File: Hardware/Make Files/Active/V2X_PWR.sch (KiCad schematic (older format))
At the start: 69 parts, among them P10 Board Mount 2, P11 Ficudial2, P12 Board Mount 3, P13 Ficudial3, P14 USB_A, P15 Board Mount 4, P16 Ficudial4, P17 NVM_RST, P18 NVM_RST, P19 NVM_RST, P6 Board Mount 1, P7 Ficudial1, P8 Open Source, P9 USB_u, Q11 IRF9335, Q12 IRF9335, Q13 BSS84, Q14 IRF9335, Q15 2N7000, SW2 SW_PUSH, U11 XRP6124, U12 SLG59M, U13 SLG59M, U14 XRP6124, U15 SLG59M, U16 SLG59M, U17 XRP6124, U18 SLG59M

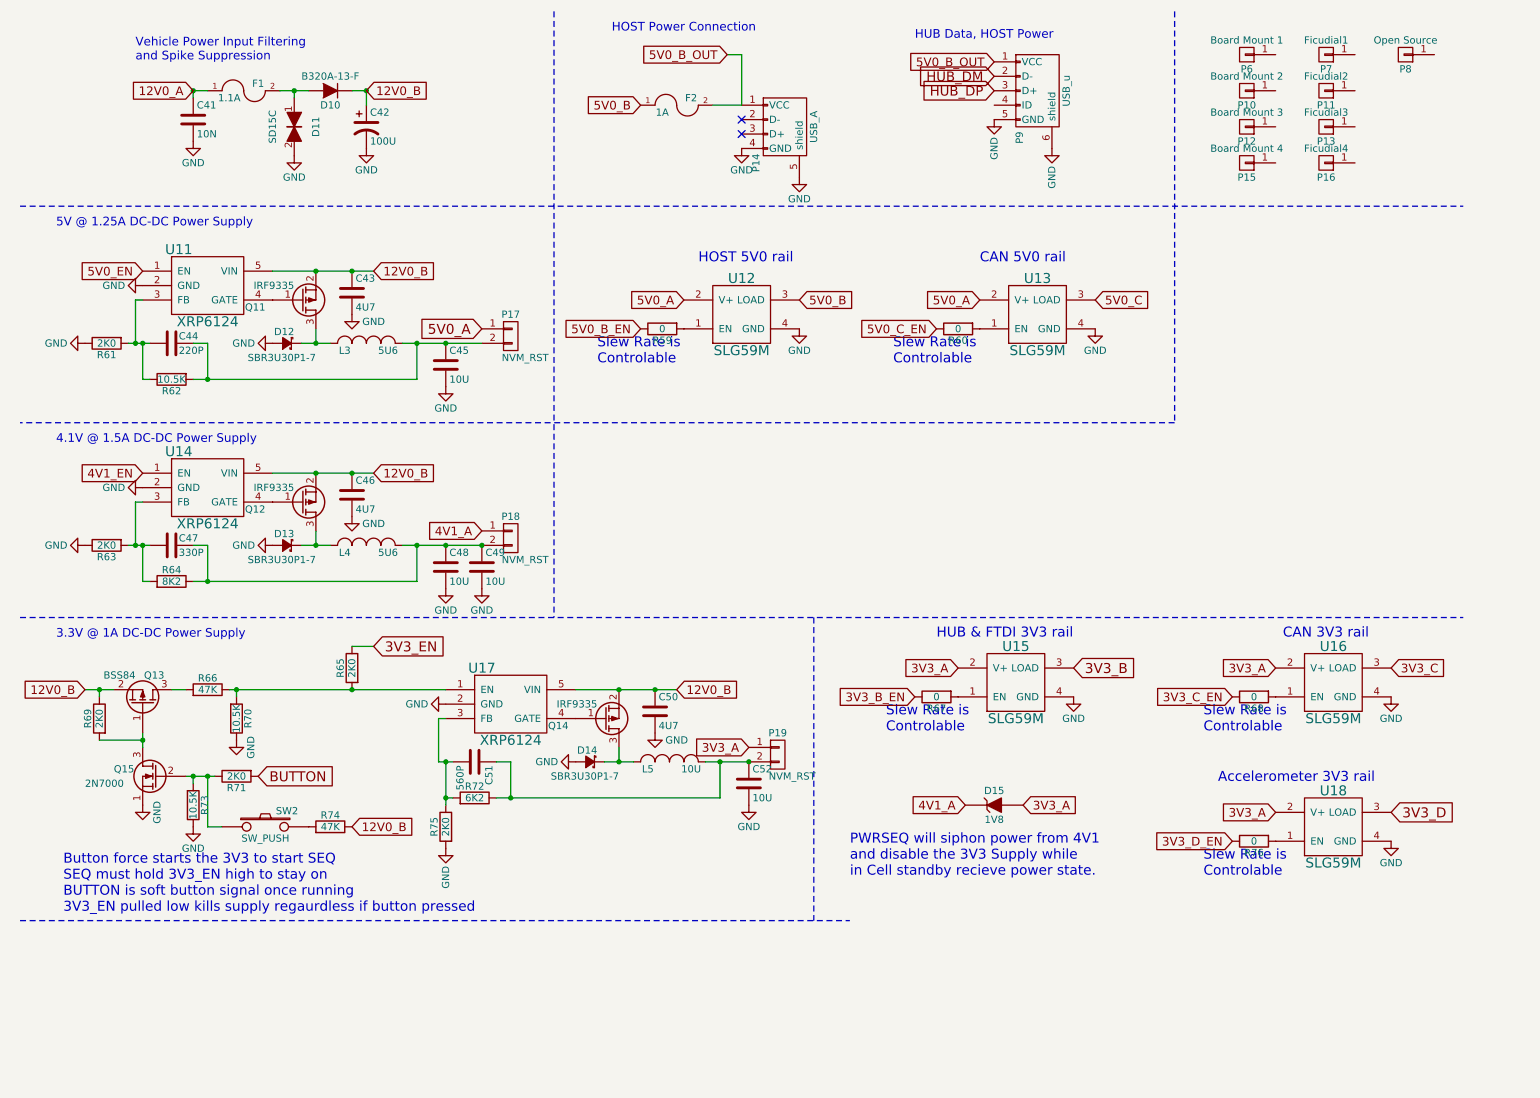
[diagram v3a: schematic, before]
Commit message: Split V2X in 2 boards, layout of SIM pcb done
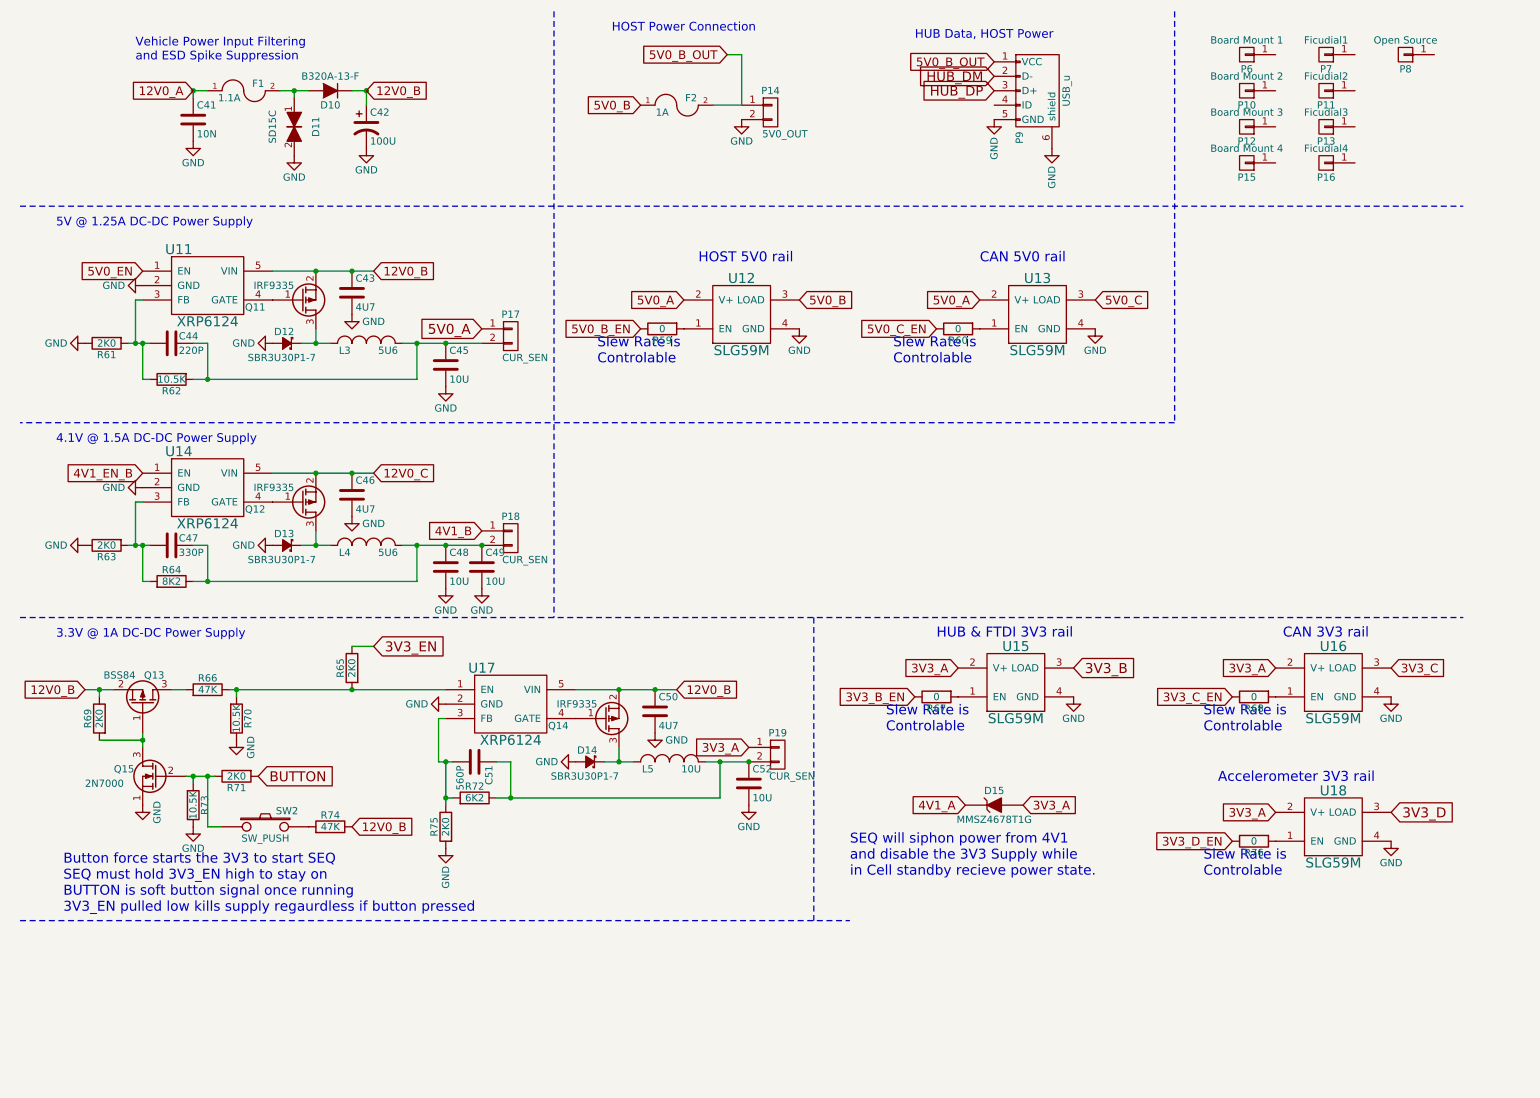
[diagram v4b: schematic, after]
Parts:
- removed P14: USB_A, Connect:USB_A, symbol USB_A
- added P14: 5V0_OUT, Connect:PINHEAD1-2, symbol CONN_01X02
- C41, C51: footprint Capacitors_SMD:C_0603 -> Custom Parts:C_0603_SM
- C43, C46, C50: footprint Capacitors_SMD:C_0603 -> Custom Parts:C_0805_SM
- C44, C47: footprint Capacitors_SMD:C_1210 -> Custom Parts:C_0603_SM
- C45, C48, C49, C52: footprint Capacitors_SMD:C_1210 -> Custom Parts:C_1206_SM
- D10: footprint Diodes_SMD:Diode-SMC_Standard -> Diodes_SMD:SMA_Standard
- D12, D13, D14: footprint (none) -> Diodes_SMD:SOD-123
- D15: value 1V8 -> MMSZ4678T1G; footprint (none) -> Diodes_SMD:SOD-123
- F2: footprint Resistors_SMD:R_1210 -> Resistors_SMD:R_1812
- L3, L4, L5: footprint (none) -> Custom Parts:4.5x4.5mm_Ind
- P17, P18, P19: value NVM_RST -> CUR_SEN
- P9: footprint Connect:USB_Micro-B -> Custom Parts:USB_Micro-B-DX4R005JJ2R1800
- Q11, Q12, Q14: footprint (none) -> Custom Parts:SOIC-8_MOS
- Q15: footprint (none) -> Housings_SOT-23_SOT-143_TSOT-6:SOT-23
- R59, R60, R61, R62, R63, R64, R65, R66, R67, R68, R69, R70, R71, R72, R73, R74, R75, R76: footprint Resistors_SMD:R_0603 -> Custom Parts:R_0603_sm
- SW2: footprint (none) -> Custom Parts:SW_SPST_FSMSM_SM
- U11, U14, U17: footprint (none) -> Housings_SOT-23_SOT-143_TSOT-6:SOT-23-5
- U12, U13, U15, U16, U18: footprint (none) -> Custom Parts:STDFN-4
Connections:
- net 12V0_B: no longer C46.1, Q12.2 (S), U14.5 (VIN)
- net 4V1_A: no longer P18.1 (P1)
- net 5V0_B_OUT: now also P14.1 (P1)
- net GND: now also P14.2 (P2)
- net 4V1_EN renamed 4V1_EN_B
- new net 12V0_C: C46.1, Q12.2 (S), U14.5 (VIN)
- new net 4V1_B: P18.1 (P1)
- no-connect marks 2 -> 0
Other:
- note added: "SEQ will siphon power from 4V1\nand disable the 3V3 Supply while \nin Cell standby recieve power state."
- note added: "Vehicle Power Input Filtering\nand ESD Spike Suppression"
- note removed: "PWRSEQ will siphon power from 4V1\nand disable the 3V3 Supply while \nin Cell standby recieve power state."
- note removed: "Vehicle Power Input Filtering\nand Spike Suppression"

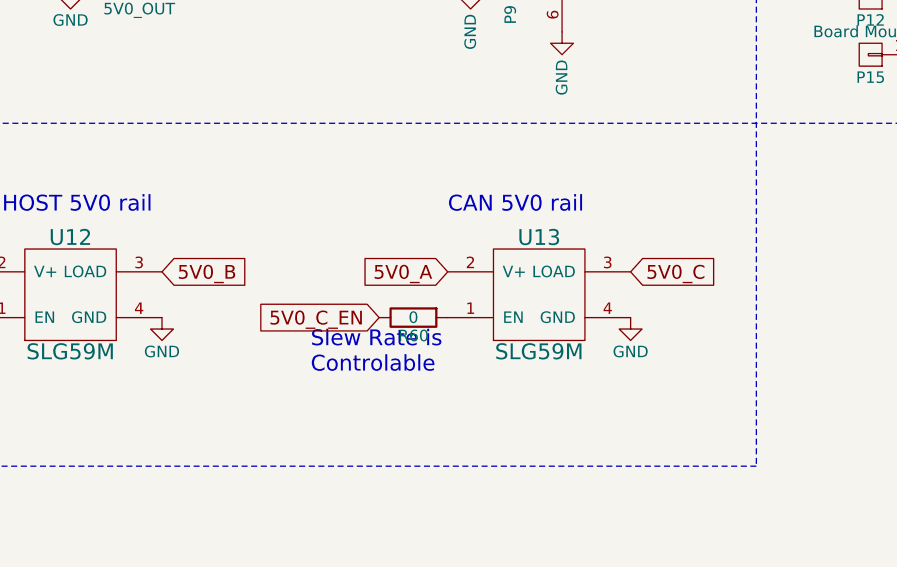
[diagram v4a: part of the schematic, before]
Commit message: Build pass of main V2X board
ready to verify
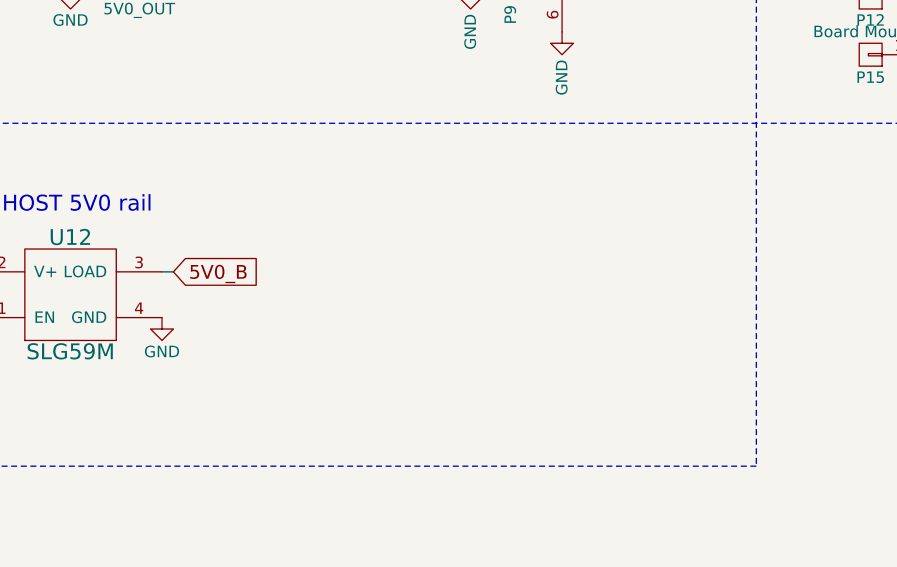
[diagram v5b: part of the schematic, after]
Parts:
- removed R60: 0, Custom Parts:R_0603_sm, symbol R
- removed U13: SLG59M, Custom Parts:STDFN-4, symbol SLG59M
- Q13, Q15: footprint Housings_SOT-23_SOT-143_TSOT-6:SOT-23 -> Custom Parts:SOT-23-123
- SW2: footprint Custom Parts:SW_SPST_FSMSM_SM -> Custom Parts:PTS645VK58-2-LFS
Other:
- note removed: "CAN 5V0 rail"
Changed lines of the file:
@@
 F 0 "SW2" H 2350 6260 50  0000 C CNN
 F 1 "SW_PUSH" H 2200 6070 50  0000 C CNN
-F 2 "Custom Parts:SW_SPST_FSMSM_SM" H 2200 6150 60  0001 C CNN
+F 2 "Custom Parts:PTS645VK58-2-LFS" H 2200 6150 60  0001 C CNN
 F 3 "http://www.mouser.com/ds/2/418/NG_CD_1437566-3_C2_1437566_3_1_c.dwg-116271.pdf" H 2200 6150 60  0001 C CNN
 F 4 "506-FSMSM" H 2200 6150 60  0001 C CNN "Mouse PN"
@@
 Text GLabel 950  5200 0    60   Input ~ 0
 12V0_B
-Text GLabel 5900 2500 2    60   Input ~ 0
+Text GLabel 5950 2500 2    60   Input ~ 0
 5V0_B
 Text GLabel 4800 1150 0    60   Input ~ 0
@@
 Text Notes 9250 4850 0    69   ~ 0
 CAN 3V3 rail
-Text GLabel 7150 2500 0    60   Input ~ 0
-5V0_A
-Text GLabel 6850 2700 0    60   Input ~ 0
-5V0_C_EN
-$Comp
-L GND #PWR0127
-U 1 1 5602FEC6
-P 7950 2700
-F 0 "#PWR0127" H 7950 2450 50  0001 C CNN
-F 1 "GND" H 7950 2550 50  0000 C CNN
-F 2 "" H 7950 2700 60  0000 C CNN
-F 3 "" H 7950 2700 60  0000 C CNN
-	1    7950 2700
-	1    0    0    -1
-$EndComp
-Text GLabel 7950 2500 2    60   Input ~ 0
-5V0_C
-Text Notes 6550 2950 0    69   ~ 0
-Slew Rate is\nControlable
-Text Notes 7150 2250 0    69   ~ 0
-CAN 5V0 rail
 Text Notes 5200 2250 0    69   ~ 0
 HOST 5V0 rail
@@
 $EndComp
 $Comp
-L SLG59M U13
-U 1 1 56056DDD
-P 7550 2600
-F 0 "U13" H 7550 2350 69  0000 C CNN
-F 1 "SLG59M" H 7550 2850 69  0000 C CNN
-F 2 "Custom Parts:STDFN-4" H 7550 2600 69  0001 C CNN
-F 3 "http://www.mouser.com/ds/2/665/SLG59M1440r111_12112013-463792.pdf" H 7550 2600 69  0001 C CNN
-F 4 "402-SLG59M1440V" H 7550 2600 60  0001 C CNN "Mouse PN"
-	1    7550 2600
-	1    0    0    1
-$EndComp
-$Comp
 L CONN_01X02 P19
 U 1 1 5607345C
@@
 $EndComp
 $Comp
-L R R60
-U 1 1 5607F2D8
-P 7000 2700
-F 0 "R60" V 7080 2700 50  0000 C CNN
-F 1 "0" V 7000 2700 50  0000 C CNN
-F 2 "Custom Parts:R_0603_sm" V 6930 2700 30  0001 C CNN
-F 3 "http://www.mouser.com/ds/2/427/dcrcwe3-109170.pdf" H 7000 2700 30  0001 C CNN
-F 4 "71-CRCW0603-0-E3" H 7000 2700 60  0001 C CNN "Mouse PN"
-	1    7000 2700
-	0    -1   1    0
-$EndComp
-$Comp
 L R R67
 U 1 1 5607F3FA
@@
 F 0 "Q13" V 1550 5450 50  0000 R CNN
 F 1 "BSS84" V 1550 5250 50  0000 R CNN
-F 2 "Housings_SOT-23_SOT-143_TSOT-6:SOT-23" H 1550 5400 29  0001 C CNN
+F 2 "Custom Parts:SOT-23-123" H 1550 5400 29  0001 C CNN
 F 3 "http://www.mouser.com/ds/2/149/BSS84-39462.pdf" H 1350 5300 60  0001 C CNN
 F 4 "512-BSS84" H 1350 5300 60  0001 C CNN "Mouse PN"
@@
 F 0 "Q15" H 1750 5850 50  0000 R CNN
 F 1 "2N7000" H 1950 5750 50  0000 R CNN
-F 2 "Housings_SOT-23_SOT-143_TSOT-6:SOT-23" H 1650 5900 29  0001 C CNN
+F 2 "Custom Parts:SOT-23-123" H 1650 5900 29  0001 C CNN
 F 3 "http://www.mouser.com/ds/2/149/2N7002K-102052.pdf" H 1450 5800 60  0001 C CNN
 F 4 "512-2N7002K" H 1450 5800 60  0001 C CNN "Mouse PN"
@@
 	1    0    0    -1
 $EndComp
+Wire Wire Line
+	5900 2500 5950 2500
 $EndSCHEMATC

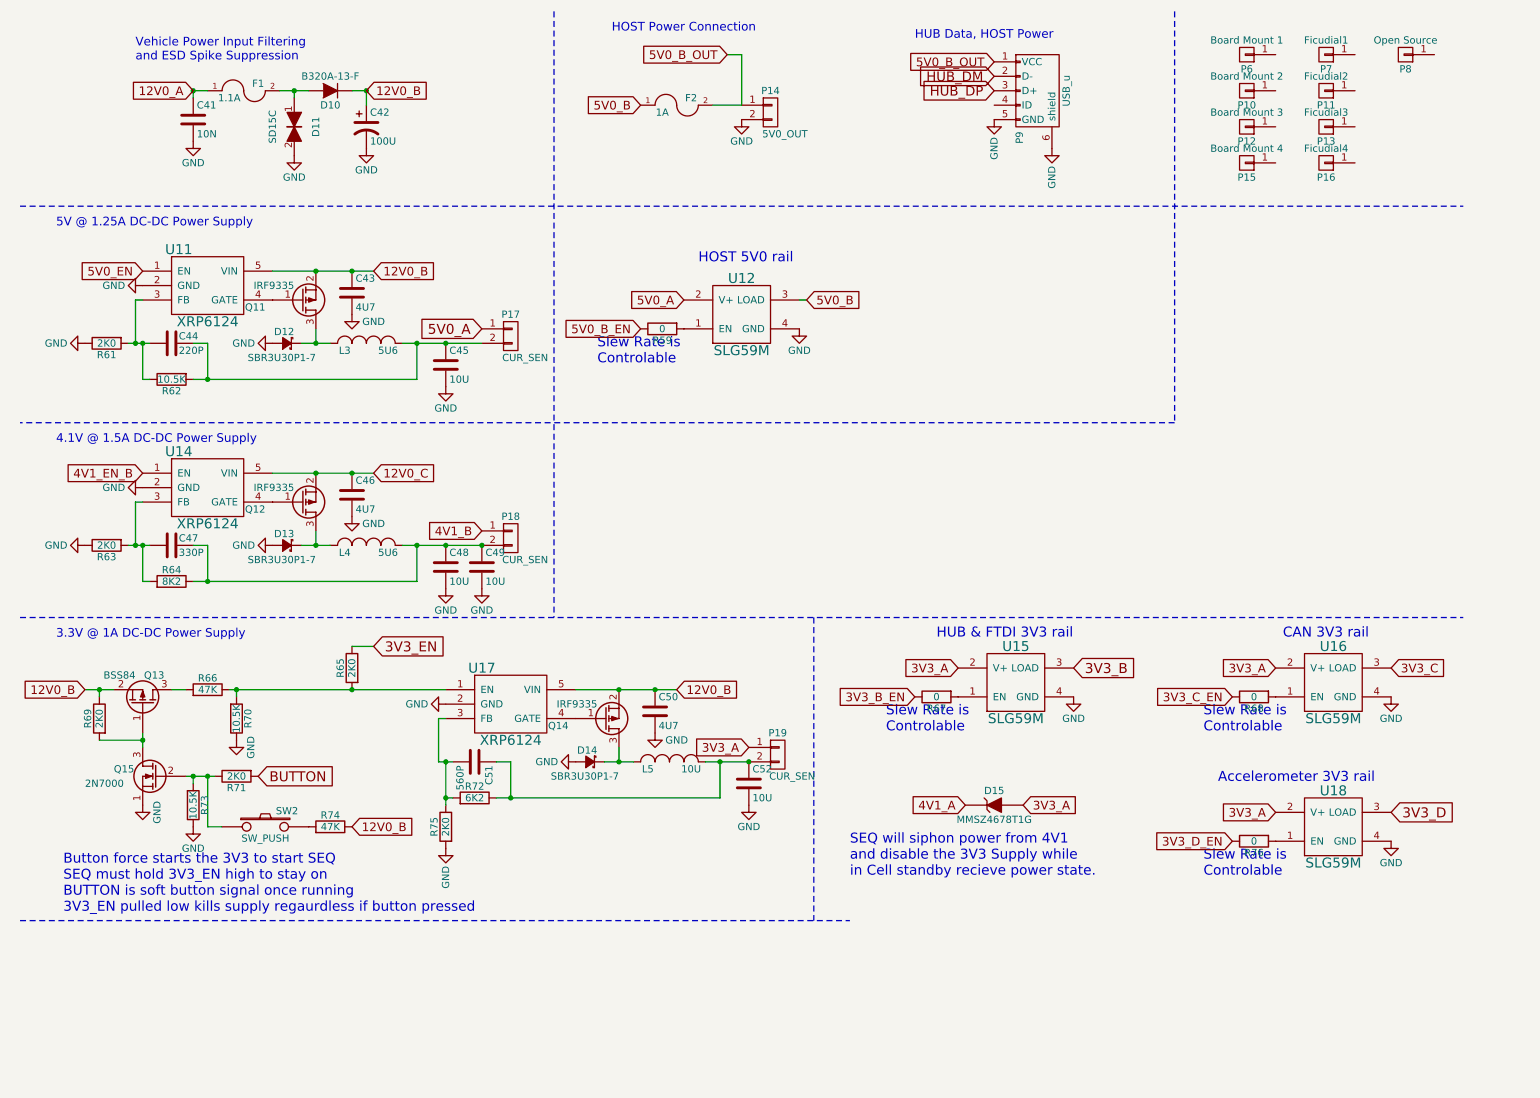
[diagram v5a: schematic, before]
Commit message: Project rework
Split the Main and GSM boards into separate projects, redesigned Main
board after flaws were found.
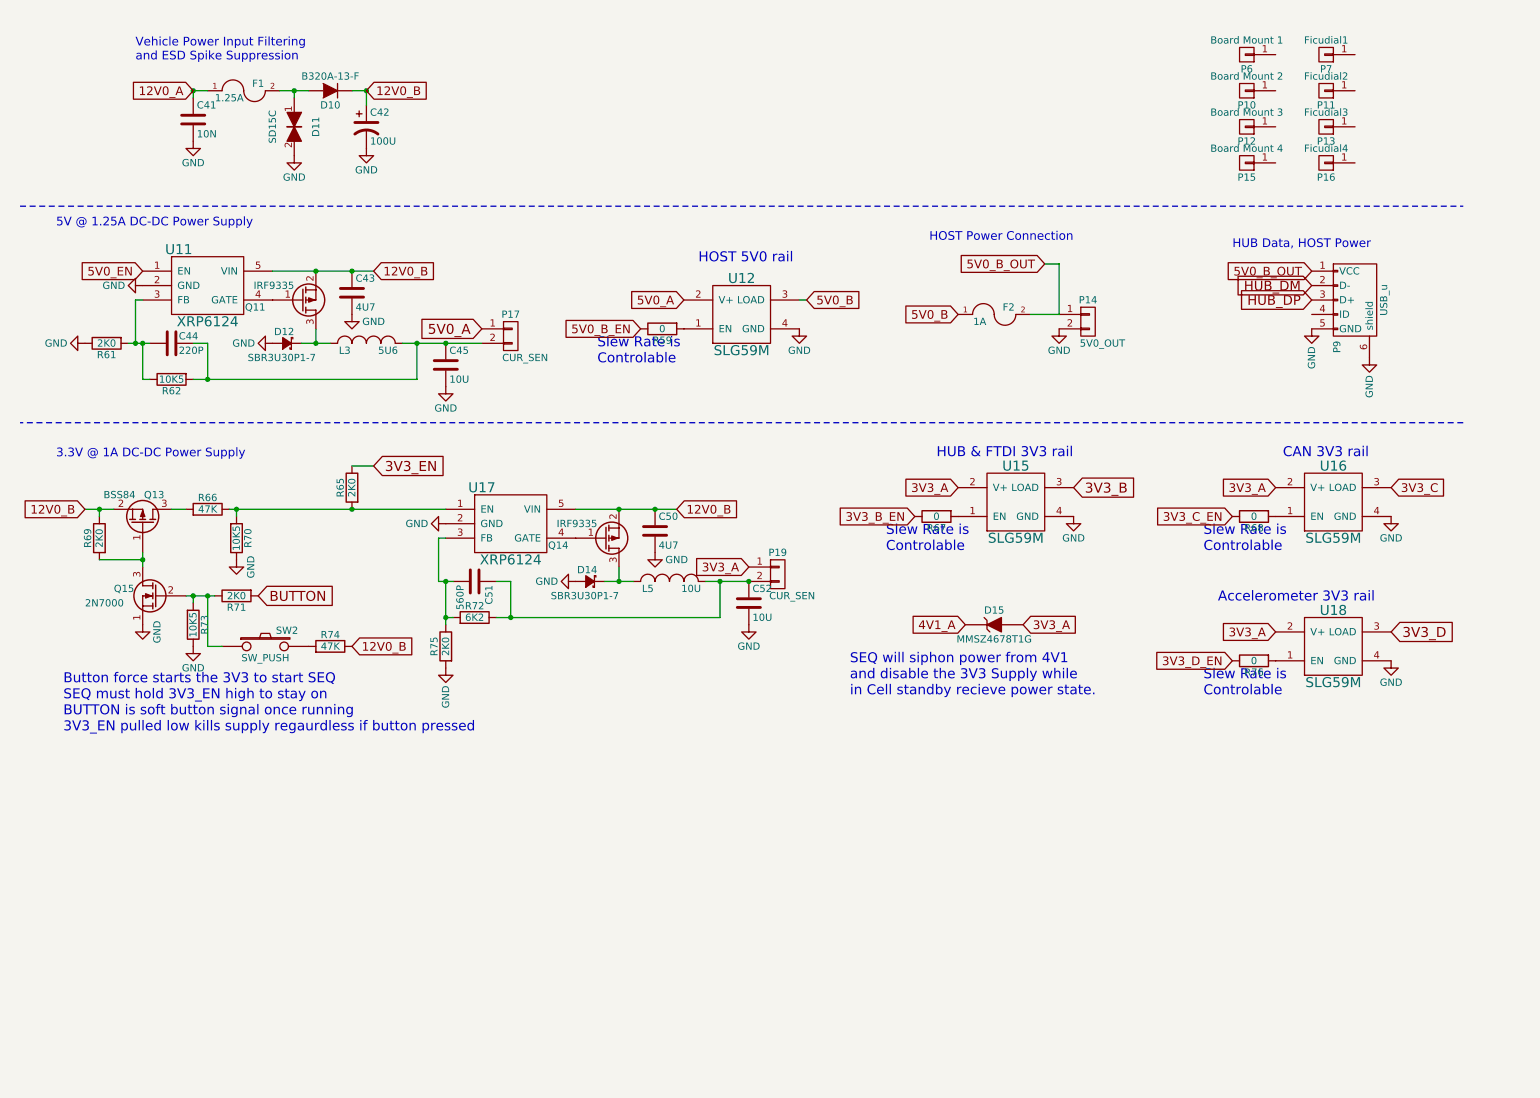
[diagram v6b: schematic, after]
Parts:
- removed C46: 4U7, Custom Parts:C_0805_SM, symbol C
- removed C47: 330P, Custom Parts:C_0603_SM, symbol C
- removed C48, C49: 10U, Custom Parts:C_1206_SM, symbol C
- removed D13: SBR3U30P1-7, Diodes_SMD:SOD-123, symbol D_Schottky_Small
- removed L4: 5U6, Custom Parts:4.5x4.5mm_Ind, symbol INDUCTOR_SMALL
- removed P18: CUR_SEN, Connect:PINHEAD1-2, symbol CONN_01X02
- removed P8: Open Source, Symbols:Symbol_OSHW-Logo_CopperTop_BIG, symbol CONN_01X01
- removed Q12: IRF9335, Custom Parts:SOIC-8_MOS, symbol Q_PMOS_GSD
- removed R63: 2K0, Custom Parts:R_0603_sm, symbol R
- removed R64: 8K2, Custom Parts:R_0603_sm, symbol R
- removed U14: XRP6124, Housings_SOT-23_SOT-143_TSOT-6:SOT-23-5, symbol XRP6124
- F1: value 1.1A -> 1.25A
- R62, R70, R73: value 10.5K -> 10K5
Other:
- note removed: "4.1V @ 1.5A DC-DC Power Supply"
- moved on the sheet: C50, C51, C52, D14, D15, F2, L5, P14, P19, P9, Q13, Q14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
